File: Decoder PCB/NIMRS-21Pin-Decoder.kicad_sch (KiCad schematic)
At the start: 89 parts, among them J1 21Pin Loco Socket, J2 U.FL, Q1 MMDT3904, Q2 MMDT3904, U1 ESP32-S3FN8, U2 MAX98357A, U4 DRV8213DSGR, U60 TPS63070, U70 TPS63070, X1 40Mhz

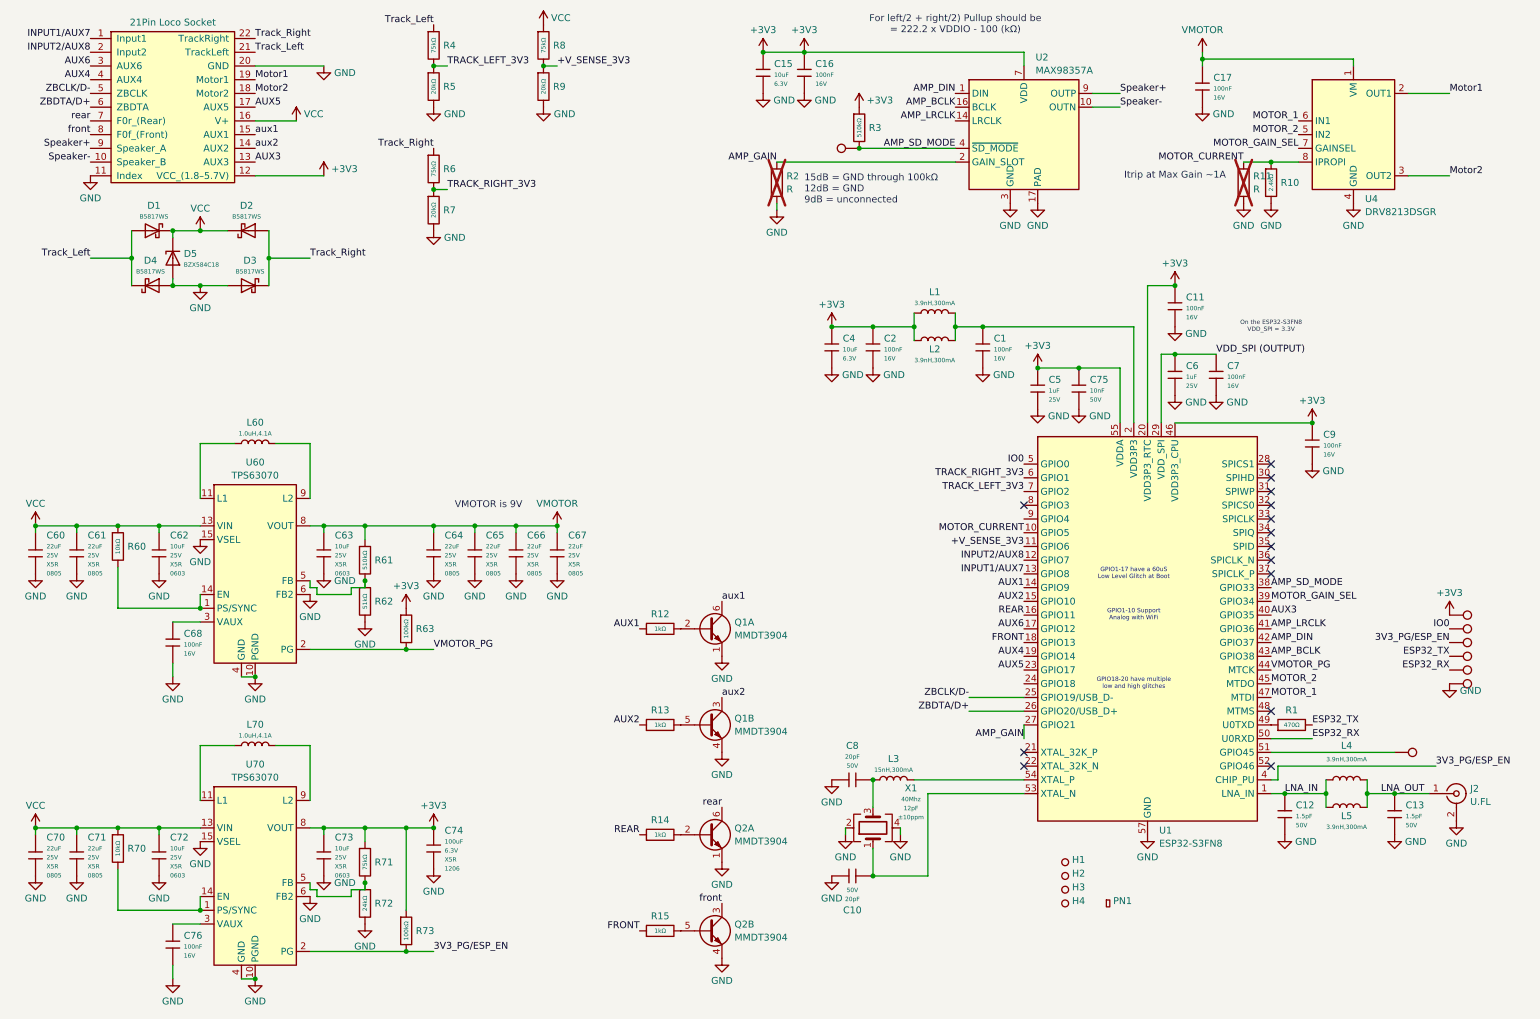
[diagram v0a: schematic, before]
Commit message: Add extra test points
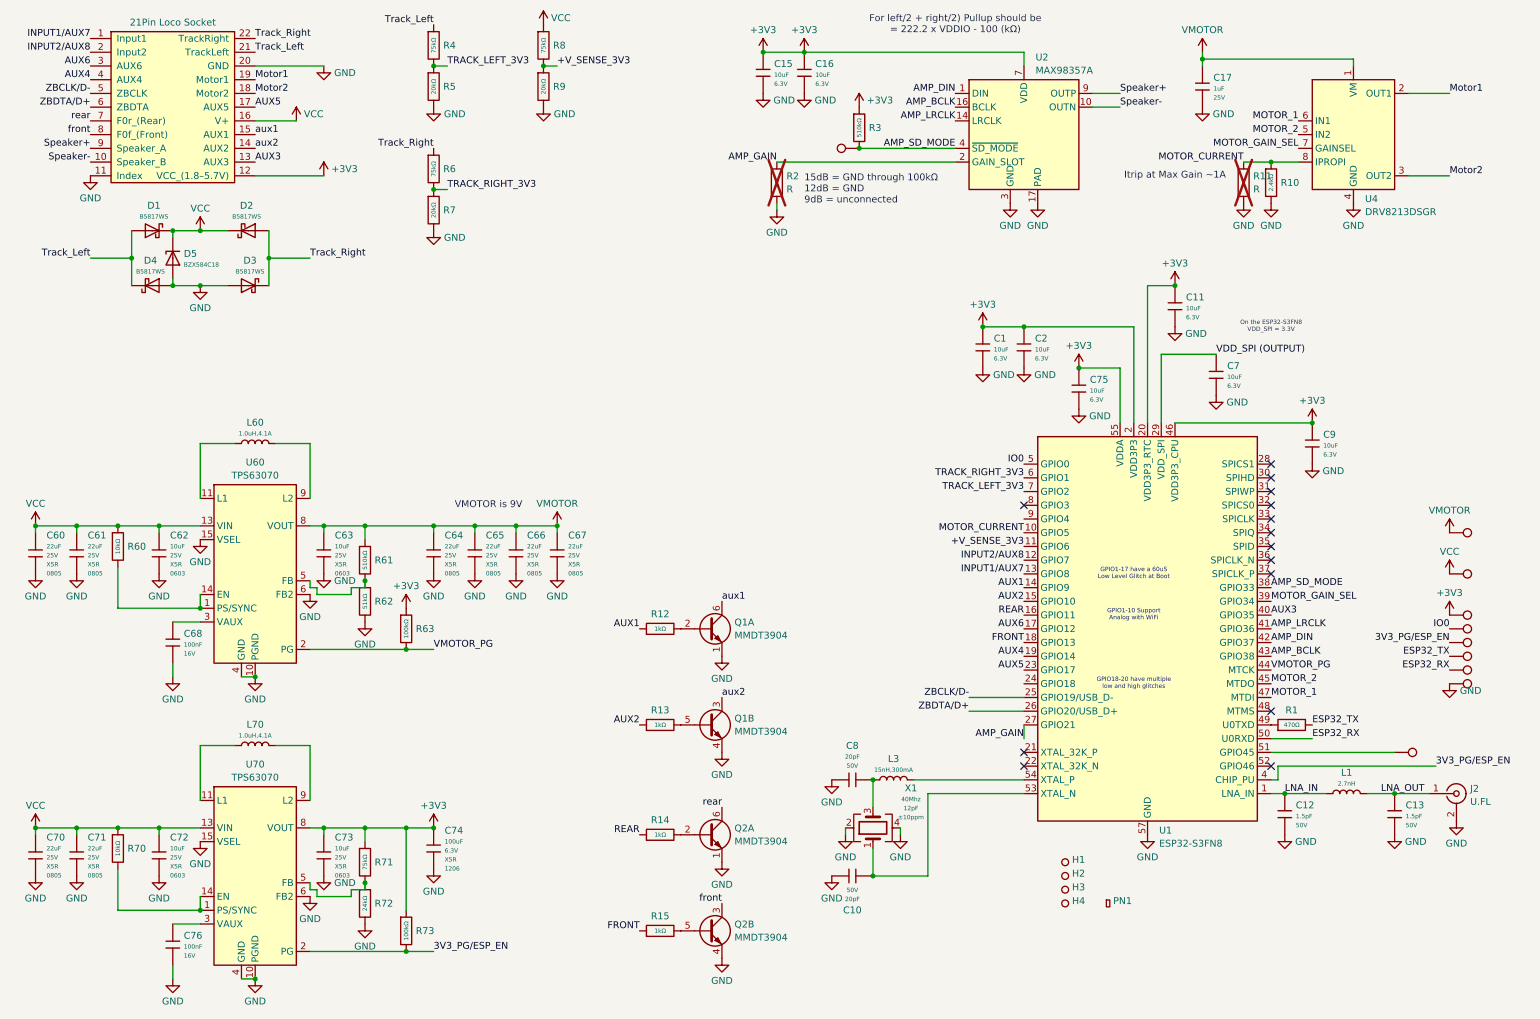
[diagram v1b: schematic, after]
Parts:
- removed C2: 100nF, PCM_JLCPCB:C_0402, symbol PCM_JLCPCB-Capacitors:0402,100nF
- removed C4: 10uF, PCM_JLCPCB:C_0402, symbol PCM_JLCPCB-Capacitors:0402,10uF
- removed C5, C6: 1uF, PCM_JLCPCB:C_0402, symbol PCM_JLCPCB-Capacitors:0402,1uF
- removed L2, L4, L5: 3.9nH,300mA, PCM_JLCPCB:L_0402, symbol PCM_JLCPCB-Inductors:3.9nH,300mA
- added C2: 10uF, PCM_JLCPCB:C_0402, symbol PCM_JLCPCB-Capacitors:0402,10uF
- added TP10, TP9: Test Point, Custom_Footprints:TestPoint_Pad_D1.0mm, symbol Connector:TestPoint
- C1, C11, C16, C7, C9: value 100nF -> 10uF; symbol PCM_JLCPCB-Capacitors:0402,100nF -> PCM_JLCPCB-Capacitors:0402,10uF; Capacitance 100nF -> 10uF; LCSC C1525 -> C15525; Part CL05B104KO5NNNC -> CL05A106MQ5NUNC; Price 0.004USD -> 0.008USD; Stock 11234519 -> 3269186; Temperature Coefficient X7R -> X5R; Tolerance ±10% -> ±20%; Voltage Rated 16V -> 6.3V
- C17: value 100nF -> 1uF; symbol PCM_JLCPCB-Capacitors:0402,100nF -> PCM_JLCPCB-Capacitors:0402,1uF; Capacitance 100nF -> 1uF; LCSC C1525 -> C52923; Part CL05B104KO5NNNC -> CL05A105KA5NQNC; Price 0.004USD -> 0.006USD; Stock 11234519 -> 5350277; Temperature Coefficient X7R -> X5R; Voltage Rated 16V -> 25V
- C75: value 10nF -> 10uF; symbol PCM_JLCPCB-Capacitors:0402,10nF -> PCM_JLCPCB-Capacitors:0402,10uF; Capacitance 10nF -> 10uF; LCSC C15195 -> C15525; Part CL05B103KB5NNNC -> CL05A106MQ5NUNC; Price 0.005USD -> 0.008USD; Stock 2778053 -> 3269186; Temperature Coefficient X7R -> X5R; Tolerance ±10% -> ±20%; Voltage Rated 50V -> 6.3V
- L1: value 3.9nH,300mA -> 2.7nH; Attrition Qty 10 -> (none); Category Inductors/Coils/Transformers,Inductors (SMD) -> (none); Class Preferred Component -> (none); DC Resistance (DCR) 200mΩ -> (none); Frequency - Self Resonant 4GHz -> (none); Inductance 3.9nH -> (none); LCSC C14033 -> C77108; Manufacturer Sunlord -> Murata Electronics; Minimum Qty 20 -> (none); Part SDCL1005C3N9STDF -> LQG15HS2N7S02D; Price 0.007USD -> (none); Q @ Freq 8@100MHz -> (none); Rated Current 300mA -> (none); Stock 50433 -> (none)
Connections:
- net +3V3: now also C1.1, U1.2 (VDD3P3), U1.3 (VDD3P3), C2.1; no longer L1.1
- net GND: now also C2.2
- net LNA_IN: now also L1.1
- net LNA_OUT: now also L1.2
- net VCC: now also TP9.1
- net VMOTOR: now also TP10.1
